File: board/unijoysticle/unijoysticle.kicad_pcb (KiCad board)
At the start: 2 copper layers, 9 parts, among them J1 DB9_Female_MountingHoles, J2 DB9_Female_MountingHoles, J3 Barrel_Jack_MountingPin, U1 4066, U2 4066, U4 4066, U5 4066

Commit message: board: new layout... WIP
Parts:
- moved D1 27.3 mm to (163.8, 110.5)
- moved U1 22.9 mm to (111.8, 86.4)
- moved U4 22.9 mm to (165.1, 86.4)
- moved U5 22.5 mm to (144.8, 94.0), turned to 90 degrees
- moved U2 15.3 mm to (124.5, 94.0), turned to 90 degrees
- moved J3 12.8 mm to (163.8, 121.9)
- moved B1 11.5 mm to (128.3, 135.9)
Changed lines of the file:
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@@
   )
   (module Parts:MH-ET_LIVE_MINIKIT_ESP32 (layer F.Cu)
-    (at 127 124.46)
+    (at 128.27 135.89)
     (descr "SPARKFUN ESP32 THING BOARD")
     (tags "SPARKFUN ESP32 THING BOARD")
@@
   )
   (module Connector_BarrelJack:BarrelJack_Horizontal (layer F.Cu)
-    (at 165.1 134.62 180)
+    (at 163.83 121.92 180)
     (descr "DC Barrel Jack")
     (tags "Power Jack")
@@
   )
   (module Diode_THT:D_DO-41_SOD81_P7.62mm_Horizontal (layer F.Cu)
-    (at 151.13 134.62)
+    (at 163.83 110.49)
     (descr "Diode, DO-41_SOD81 series, Axial, Horizontal, pin pitch=7.62mm, , length*diameter=5.2*2.7mm^2, , http://www.diodes.com/_files/packages/DO-41%20(Plastic).pdf")
     (tags "Diode DO-41_SOD81 series Axial Horizontal pin pitch 7.62mm  length 5.2mm diameter 2.7mm")
@@
   )
   (module Package_DIP:DIP-14_W7.62mm_Socket_LongPads (layer F.Cu)
-    (at 166.37 87.63)
+    (at 144.78 93.98 90)
     (descr "14-lead though-hole mounted DIP package, row spacing 7.62 mm (300 mils), Socket, LongPads")
     (tags "THT DIP DIL PDIP 2.54mm 7.62mm 300mil Socket LongPads")
-    (fp_text reference U5 (at 3.81 -2.33) (layer F.SilkS)
-      (effects (font (size 1 1) (thickness 0.15)))
-    )
-    (fp_text value 4066 (at 3.81 17.57) (layer F.Fab)
-      (effects (font (size 1 1) (thickness 0.15)))
-    )
-    (fp_text user %R (at 3.81 7.62) (layer F.Fab)
+    (fp_text reference U5 (at 3.81 -2.33 90) (layer F.SilkS)
+      (effects (font (size 1 1) (thickness 0.15)))
+    )
+    (fp_text value 4066 (at 3.81 17.57 90) (layer F.Fab)
+      (effects (font (size 1 1) (thickness 0.15)))
+    )
+    (fp_text user %R (at 3.81 7.62 90) (layer F.Fab)
       (effects (font (size 1 1) (thickness 0.15)))
     )
@@
     (fp_line (start 1.635 -1.27) (end 6.985 -1.27) (layer F.Fab) (width 0.1))
     (fp_arc (start 3.81 -1.33) (end 2.81 -1.33) (angle -180) (layer F.SilkS) (width 0.12))
-    (pad 14 thru_hole oval (at 7.62 0) (size 2.4 1.6) (drill 0.8) (layers *.Cu *.Mask)
+    (pad 14 thru_hole oval (at 7.62 0 90) (size 2.4 1.6) (drill 0.8) (layers *.Cu *.Mask)
       (net 22 Vdd))
-    (pad 7 thru_hole oval (at 0 15.24) (size 2.4 1.6) (drill 0.8) (layers *.Cu *.Mask)
+    (pad 7 thru_hole oval (at 0 15.24 90) (size 2.4 1.6) (drill 0.8) (layers *.Cu *.Mask)
       (net 21 Vss))
-    (pad 13 thru_hole oval (at 7.62 2.54) (size 2.4 1.6) (drill 0.8) (layers *.Cu *.Mask)
+    (pad 13 thru_hole oval (at 7.62 2.54 90) (size 2.4 1.6) (drill 0.8) (layers *.Cu *.Mask)
       (net 8 GPIO_J2FIRE))
-    (pad 6 thru_hole oval (at 0 12.7) (size 2.4 1.6) (drill 0.8) (layers *.Cu *.Mask)
+    (pad 6 thru_hole oval (at 0 12.7 90) (size 2.4 1.6) (drill 0.8) (layers *.Cu *.Mask)
       (net 12 GPIO_J2POTY))
-    (pad 12 thru_hole oval (at 7.62 5.08) (size 2.4 1.6) (drill 0.8) (layers *.Cu *.Mask))
-    (pad 5 thru_hole oval (at 0 10.16) (size 2.4 1.6) (drill 0.8) (layers *.Cu *.Mask)
+    (pad 12 thru_hole oval (at 7.62 5.08 90) (size 2.4 1.6) (drill 0.8) (layers *.Cu *.Mask))
+    (pad 5 thru_hole oval (at 0 10.16 90) (size 2.4 1.6) (drill 0.8) (layers *.Cu *.Mask)
       (net 13 GPIO_J2POTX))
-    (pad 11 thru_hole oval (at 7.62 7.62) (size 2.4 1.6) (drill 0.8) (layers *.Cu *.Mask))
-    (pad 4 thru_hole oval (at 0 7.62) (size 2.4 1.6) (drill 0.8) (layers *.Cu *.Mask)
+    (pad 11 thru_hole oval (at 7.62 7.62 90) (size 2.4 1.6) (drill 0.8) (layers *.Cu *.Mask))
+    (pad 4 thru_hole oval (at 0 7.62 90) (size 2.4 1.6) (drill 0.8) (layers *.Cu *.Mask)
       (net 31 J2POTX))
-    (pad 10 thru_hole oval (at 7.62 10.16) (size 2.4 1.6) (drill 0.8) (layers *.Cu *.Mask))
-    (pad 3 thru_hole oval (at 0 5.08) (size 2.4 1.6) (drill 0.8) (layers *.Cu *.Mask)
+    (pad 10 thru_hole oval (at 7.62 10.16 90) (size 2.4 1.6) (drill 0.8) (layers *.Cu *.Mask))
+    (pad 3 thru_hole oval (at 0 5.08 90) (size 2.4 1.6) (drill 0.8) (layers *.Cu *.Mask)
       (net 24 VDD))
-    (pad 9 thru_hole oval (at 7.62 12.7) (size 2.4 1.6) (drill 0.8) (layers *.Cu *.Mask)
+    (pad 9 thru_hole oval (at 7.62 12.7 90) (size 2.4 1.6) (drill 0.8) (layers *.Cu *.Mask)
       (net 24 VDD))
-    (pad 2 thru_hole oval (at 0 2.54) (size 2.4 1.6) (drill 0.8) (layers *.Cu *.Mask)
-      (net 1 GND))
-    (pad 8 thru_hole oval (at 7.62 15.24) (size 2.4 1.6) (drill 0.8) (layers *.Cu *.Mask)
+    (pad 2 thru_hole oval (at 0 2.54 90) (size 2.4 1.6) (drill 0.8) (layers *.Cu *.Mask)
+      (net 1 GND))
+    (pad 8 thru_hole oval (at 7.62 15.24 90) (size 2.4 1.6) (drill 0.8) (layers *.Cu *.Mask)
       (net 32 J2POTY))
-    (pad 1 thru_hole rect (at 0 0) (size 2.4 1.6) (drill 0.8) (layers *.Cu *.Mask)
+    (pad 1 thru_hole rect (at 0 0 90) (size 2.4 1.6) (drill 0.8) (layers *.Cu *.Mask)
       (net 33 J2FIRE))
     (model ${KISYS3DMOD}/Package_DIP.3dshapes/DIP-14_W7.62mm_Socket.wrl
@@
   )
   (module Package_DIP:DIP-14_W7.62mm_Socket_LongPads (layer F.Cu)
-    (at 166.37 109.22)
+    (at 165.1 86.36)
     (descr "14-lead though-hole mounted DIP package, row spacing 7.62 mm (300 mils), Socket, LongPads")
     (tags "THT DIP DIL PDIP 2.54mm 7.62mm 300mil Socket LongPads")
@@
   )
   (module Package_DIP:DIP-14_W7.62mm_Socket_LongPads (layer F.Cu)
-    (at 110.49 87.63)
+    (at 124.46 93.98 90)
     (descr "14-lead though-hole mounted DIP package, row spacing 7.62 mm (300 mils), Socket, LongPads")
     (tags "THT DIP DIL PDIP 2.54mm 7.62mm 300mil Socket LongPads")
-    (fp_text reference U2 (at 3.81 -2.33) (layer F.SilkS)
-      (effects (font (size 1 1) (thickness 0.15)))
-    )
-    (fp_text value 4066 (at 3.81 17.57) (layer F.Fab)
-      (effects (font (size 1 1) (thickness 0.15)))
-    )
-    (fp_text user %R (at 3.81 7.62) (layer F.Fab)
+    (fp_text reference U2 (at 3.81 -2.33 90) (layer F.SilkS)
+      (effects (font (size 1 1) (thickness 0.15)))
+    )
+    (fp_text value 4066 (at 3.81 17.57 90) (layer F.Fab)
+      (effects (font (size 1 1) (thickness 0.15)))
+    )
+    (fp_text user %R (at 3.81 7.62 90) (layer F.Fab)
       (effects (font (size 1 1) (thickness 0.15)))
     )
@@
     (fp_line (start 1.635 -1.27) (end 6.985 -1.27) (layer F.Fab) (width 0.1))
     (fp_arc (start 3.81 -1.33) (end 2.81 -1.33) (angle -180) (layer F.SilkS) (width 0.12))
-    (pad 14 thru_hole oval (at 7.62 0) (size 2.4 1.6) (drill 0.8) (layers *.Cu *.Mask)
+    (pad 14 thru_hole oval (at 7.62 0 90) (size 2.4 1.6) (drill 0.8) (layers *.Cu *.Mask)
       (net 22 Vdd))
-    (pad 7 thru_hole oval (at 0 15.24) (size 2.4 1.6) (drill 0.8) (layers *.Cu *.Mask)
+    (pad 7 thru_hole oval (at 0 15.24 90) (size 2.4 1.6) (drill 0.8) (layers *.Cu *.Mask)
       (net 21 Vss))
-    (pad 13 thru_hole oval (at 7.62 2.54) (size 2.4 1.6) (drill 0.8) (layers *.Cu *.Mask)
+    (pad 13 thru_hole oval (at 7.62 2.54 90) (size 2.4 1.6) (drill 0.8) (layers *.Cu *.Mask)
       (net 14 GPIO_J1FIRE))
-    (pad 6 thru_hole oval (at 0 12.7) (size 2.4 1.6) (drill 0.8) (layers *.Cu *.Mask)
+    (pad 6 thru_hole oval (at 0 12.7 90) (size 2.4 1.6) (drill 0.8) (layers *.Cu *.Mask)
       (net 6 GPIO_J1POTY))
-    (pad 12 thru_hole oval (at 7.62 5.08) (size 2.4 1.6) (drill 0.8) (layers *.Cu *.Mask))
-    (pad 5 thru_hole oval (at 0 10.16) (size 2.4 1.6) (drill 0.8) (layers *.Cu *.Mask)
+    (pad 12 thru_hole oval (at 7.62 5.08 90) (size 2.4 1.6) (drill 0.8) (layers *.Cu *.Mask))
+    (pad 5 thru_hole oval (at 0 10.16 90) (size 2.4 1.6) (drill 0.8) (layers *.Cu *.Mask)
       (net 3 GPIO_J1POTX))
-    (pad 11 thru_hole oval (at 7.62 7.62) (size 2.4 1.6) (drill 0.8) (layers *.Cu *.Mask))
-    (pad 4 thru_hole oval (at 0 7.62) (size 2.4 1.6) (drill 0.8) (layers *.Cu *.Mask)
+    (pad 11 thru_hole oval (at 7.62 7.62 90) (size 2.4 1.6) (drill 0.8) (layers *.Cu *.Mask))
+    (pad 4 thru_hole oval (at 0 7.62 90) (size 2.4 1.6) (drill 0.8) (layers *.Cu *.Mask)
       (net 23 J1POTX))
-    (pad 10 thru_hole oval (at 7.62 10.16) (size 2.4 1.6) (drill 0.8) (layers *.Cu *.Mask))
-    (pad 3 thru_hole oval (at 0 5.08) (size 2.4 1.6) (drill 0.8) (layers *.Cu *.Mask)
+    (pad 10 thru_hole oval (at 7.62 10.16 90) (size 2.4 1.6) (drill 0.8) (layers *.Cu *.Mask))
+    (pad 3 thru_hole oval (at 0 5.08 90) (size 2.4 1.6) (drill 0.8) (layers *.Cu *.Mask)
       (net 24 VDD))
-    (pad 9 thru_hole oval (at 7.62 12.7) (size 2.4 1.6) (drill 0.8) (layers *.Cu *.Mask)
+    (pad 9 thru_hole oval (at 7.62 12.7 90) (size 2.4 1.6) (drill 0.8) (layers *.Cu *.Mask)
       (net 24 VDD))
-    (pad 2 thru_hole oval (at 0 2.54) (size 2.4 1.6) (drill 0.8) (layers *.Cu *.Mask)
-      (net 1 GND))
-    (pad 8 thru_hole oval (at 7.62 15.24) (size 2.4 1.6) (drill 0.8) (layers *.Cu *.Mask)
+    (pad 2 thru_hole oval (at 0 2.54 90) (size 2.4 1.6) (drill 0.8) (layers *.Cu *.Mask)
+      (net 1 GND))
+    (pad 8 thru_hole oval (at 7.62 15.24 90) (size 2.4 1.6) (drill 0.8) (layers *.Cu *.Mask)
       (net 25 J1POTY))
-    (pad 1 thru_hole rect (at 0 0) (size 2.4 1.6) (drill 0.8) (layers *.Cu *.Mask)
+    (pad 1 thru_hole rect (at 0 0 90) (size 2.4 1.6) (drill 0.8) (layers *.Cu *.Mask)
       (net 26 J1FIRE))
     (model ${KISYS3DMOD}/Package_DIP.3dshapes/DIP-14_W7.62mm_Socket.wrl
@@
   )
   (module Package_DIP:DIP-14_W7.62mm_Socket_LongPads (layer F.Cu)
-    (at 110.49 109.22)
+    (at 111.76 86.36)
     (descr "14-lead though-hole mounted DIP package, row spacing 7.62 mm (300 mils), Socket, LongPads")
     (tags "THT DIP DIL PDIP 2.54mm 7.62mm 300mil Socket LongPads")

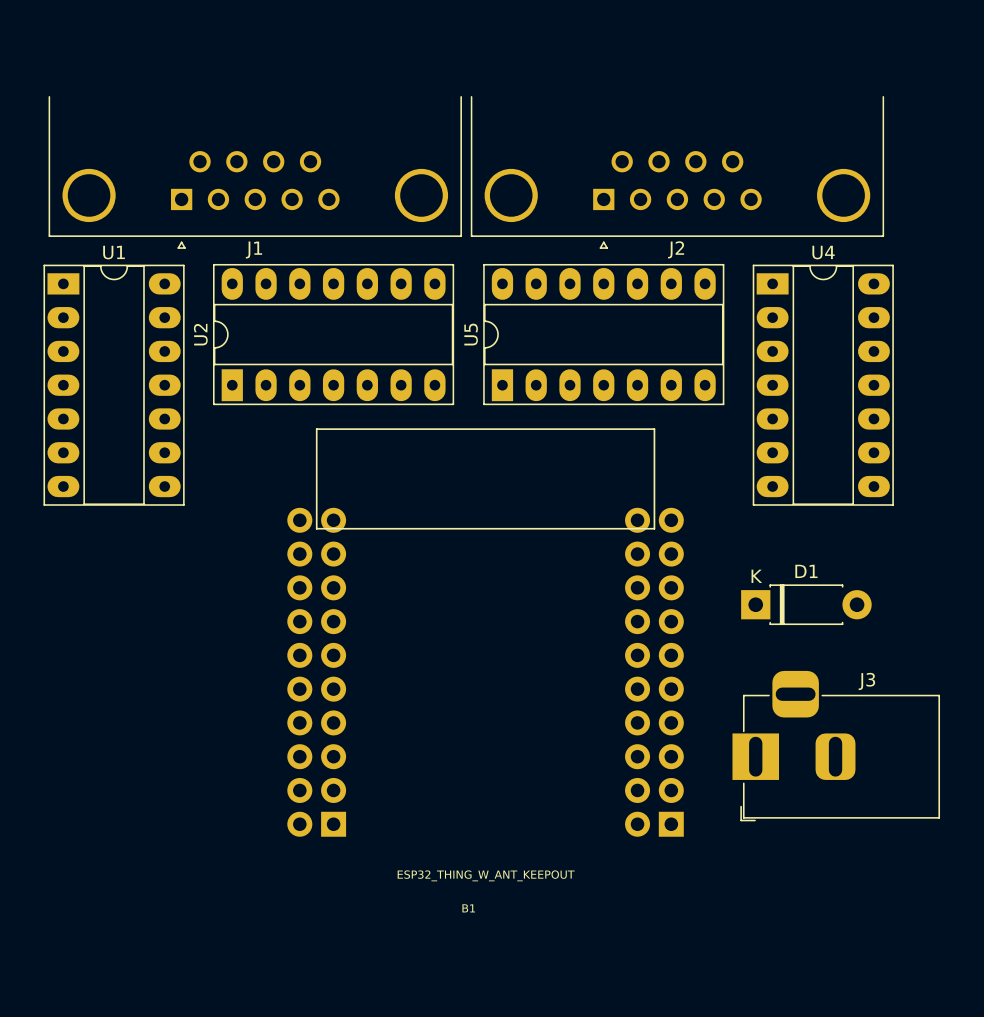
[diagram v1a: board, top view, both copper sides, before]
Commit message: board: using switch for c64/amiga mouse
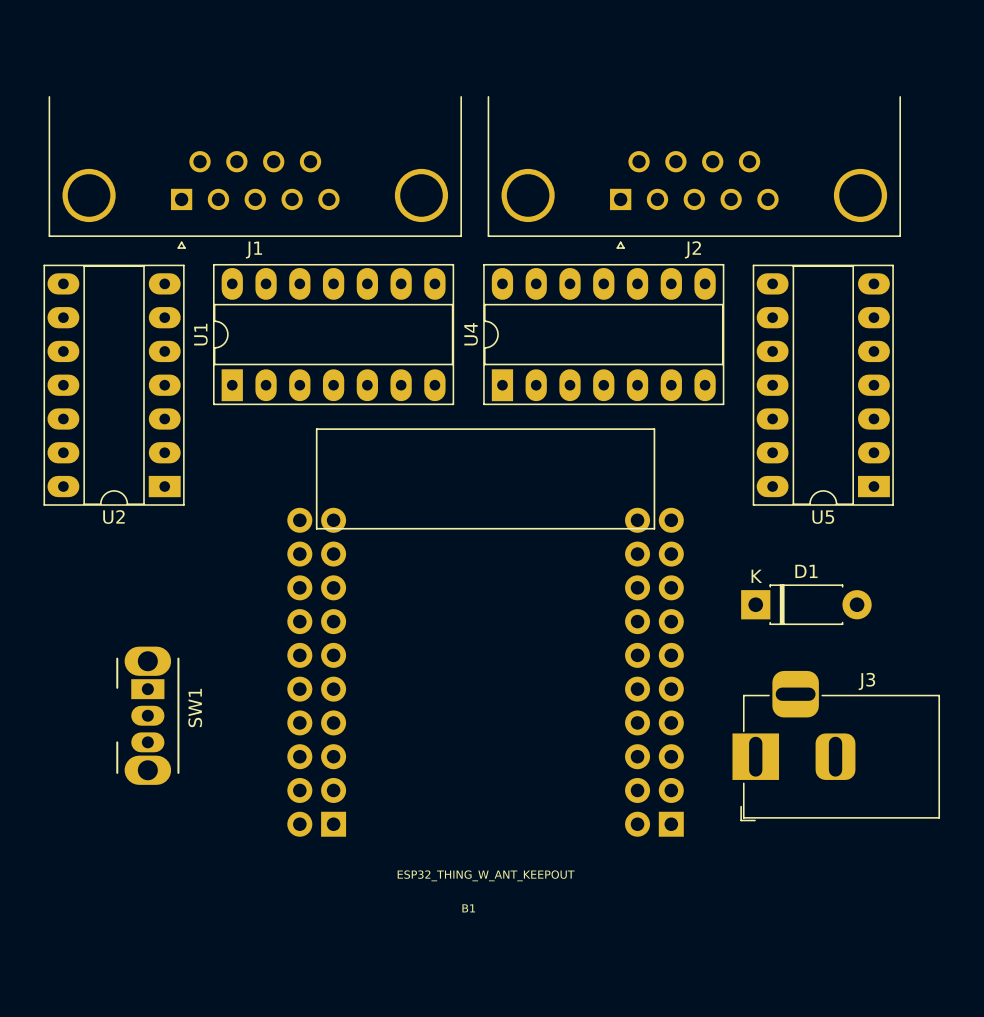
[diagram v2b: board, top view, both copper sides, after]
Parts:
- added SW1: SW_SPDT, Button_Switch_THT:SW_CuK_OS102011MA1QN1_SPDT_Angled, F.Cu at (118.1, 116.8)
- moved U5 29.0 mm to (172.7, 101.6), turned to 180 degrees
- moved U4 21.7 mm to (144.8, 94.0), turned to 90 degrees
- moved U1 14.8 mm to (124.5, 94.0), turned to 90 degrees
- moved U2 9.16 mm to (119.4, 101.6), turned to 180 degrees
- moved J2 1.27 mm to (153.7, 80.0)
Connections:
- B1 pad 2: +5V -> VDD
- D1 pad 1: +5V -> VDD
- J1 pad 7: VDD -> J1POWER
- J2 pad 7: VDD -> Net-(J2-Pad7)
- U2 pad 3: VDD -> POWER_OR_GND
- U2 pad 9: VDD -> POWER_OR_GND
- U5 pad 3: VDD -> POWER_OR_GND
- U5 pad 9: VDD -> POWER_OR_GND

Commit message: board: better layout
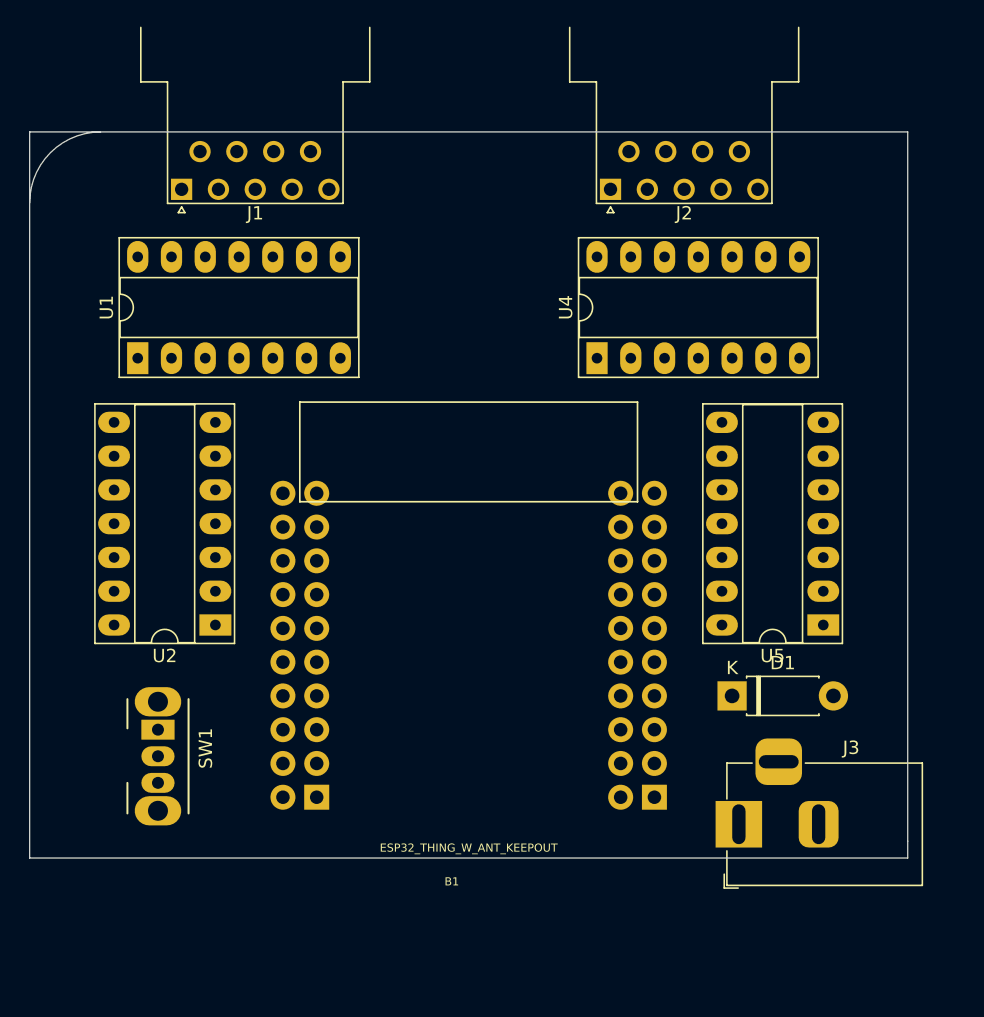
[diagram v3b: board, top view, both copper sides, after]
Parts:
- J1, J2: footprint Connector_Dsub:DSUB-9_Female_Horizontal_P2.77x2.84mm_EdgePinOffset4.94mm_Housed_MountingHolesOffset7.48mm -> Connector_Dsub:DSUB-9_Female_Horizontal_P2.77x2.84mm_EdgePinOffset9.40mm
- moved U2 11.1 mm to (123.2, 112.0)
- moved U5 11.1 mm to (168.9, 112.0)
- moved U1 7.40 mm to (117.3, 91.9)
- moved U4 7.40 mm to (151.9, 91.9)
- moved D1 7.08 mm to (162.1, 117.3)
- moved J3 5.24 mm to (162.6, 127.0)
- moved SW1 3.14 mm to (118.9, 119.9)
- moved B1 2.40 mm to (127.0, 133.9)
- moved J2 1.08 mm to (152.9, 79.2)
- moved J1 0.76 mm to (120.7, 79.2)
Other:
- board outline added: 66 x 54.6 mm
- net class Default: clearance 0.2 -> 0.1524; trace_width 0.25 -> 0.1524; via_dia 0.8 -> 0.6858; via_drill 0.4 -> 0.3302
- rule pad_to_mask_clearance: 0.051 -> 0.0508
- rule trace_clearance: 0.2 -> 0.1524
- rule trace_min: 0.2 -> 0.1524
- rule via_min_drill: 0.3 -> 0.254
- rule via_min_size: 0.4 -> 0.508

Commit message: board: routing added
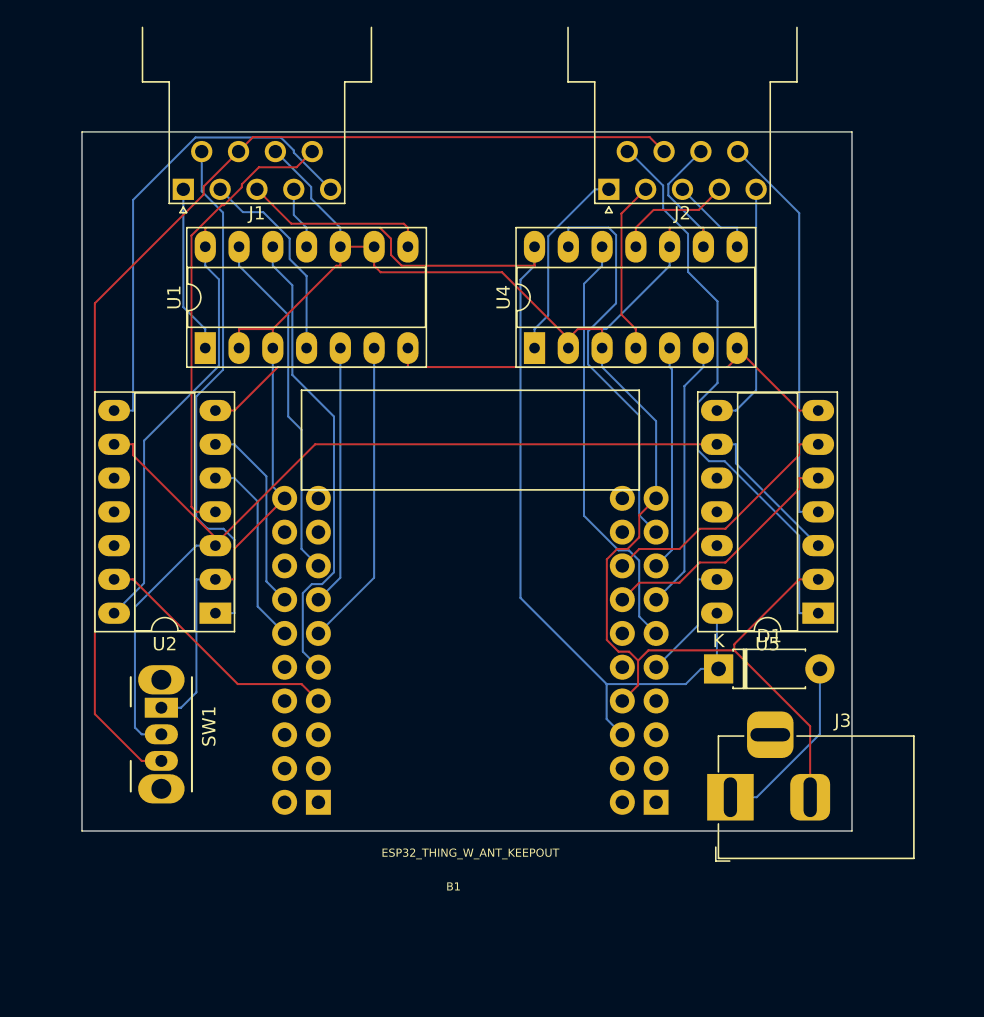
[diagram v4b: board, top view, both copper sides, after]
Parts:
- moved U1 5.14 mm to (122.4, 91.2)
- moved U4 4.76 mm to (147.2, 91.2)
- moved D1 2.27 mm to (161.0, 115.3)
- moved J3 2.13 mm to (161.9, 125.0)
- moved SW1 1.67 mm to (119.1, 118.2)
- moved U5 0.97 mm to (168.5, 111.1)
- moved U2 0.89 mm to (123.2, 111.1)
- moved B1 0.40 mm to (127.1, 134.2)
- moved J1 0.13 mm to (120.8, 79.2)
- moved J2 0.13 mm to (152.8, 79.2)
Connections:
- J2 pad 7: Net-(J2-Pad7) -> J1POWER
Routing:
- net GND: track 0.00 -> 169.3 mm
- net Vdd: track 0.00 -> 114.4 mm
- net J1POWER: track 0.00 -> 86.1 mm
- net POWER_OR_GND: track 0.00 -> 83.1 mm
- net Vss: track 0.00 -> 50.8 mm
- net J2FIRE: track 0.00 -> 43.5 mm
- net J1FIRE: track 0.00 -> 39.5 mm
- net J1POTY: track 0.00 -> 35.8 mm
- net GPIO_J1RIGHT: track 0.00 -> 35.4 mm
- net J1POTX: track 0.00 -> 34.2 mm
- net GPIO_J2RIGHT: track 0.00 -> 32.3 mm
- net GPIO_J2UP: track 0.00 -> 30.6 mm
- net J2POTX: track 0.00 -> 30.4 mm
- net GPIO_J1UP: track 0.00 -> 26.5 mm
- net GPIO_J1LEFT: track 0.00 -> 23.2 mm
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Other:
- board size 66 x 54.6 mm -> 57.9 x 52.6 mm
